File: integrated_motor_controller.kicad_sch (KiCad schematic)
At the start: 26 parts, among them J1 RCVR, J10 CH2, J2 SWD, J3 ENC 0, J4 ENC 1, J5 UART, J6 CH0, J7 I2C, J8 CH1, J9 I2C

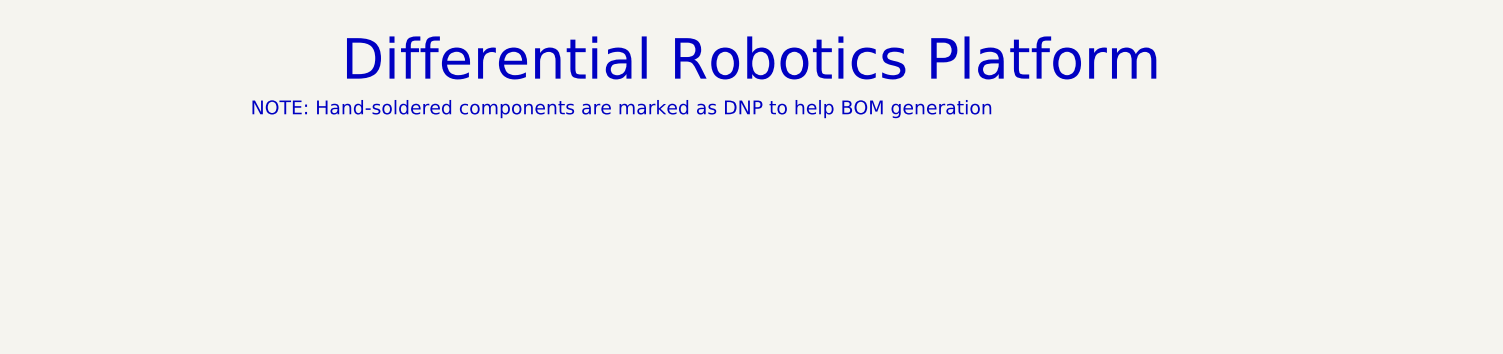
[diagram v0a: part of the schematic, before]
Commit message: Cleanup a comment in main schematic for the new project name
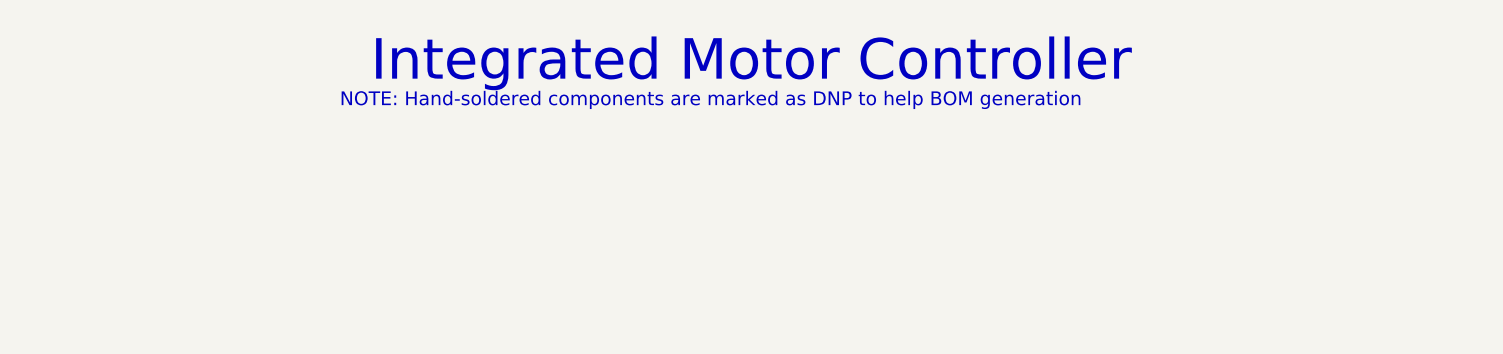
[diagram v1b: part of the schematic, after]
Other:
- note added: "Integrated Motor Controller"
- note removed: "Differential Robotics Platform"
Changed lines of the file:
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@@
 		)
 	)
-	(text "Differential Robotics Platform"
+	(text "Integrated Motor Controller"
 		(exclude_from_sim no)
 		(at 190.5 22.86 0)
@@
 	(text "NOTE: Hand-soldered components are marked as DNP to help BOM generation"
 		(exclude_from_sim no)
-		(at 134.874 28.194 0)
+		(at 144.78 27.178 0)
 		(effects
 			(font

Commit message: Final edits before sending to fab
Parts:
- added R2, R3: 3.3k, Resistor_SMD:R_0603_1608Metric, symbol Device:R_Small_US
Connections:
- net +3.3V: now also R2.2, R3.2
- net I2C_SCL: now also R2.1
- net I2C_SDA: now also R3.1
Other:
- sheet IMU: file imu_icm42688.kicad_sch -> imu_lsm6dsv.kicad_sch

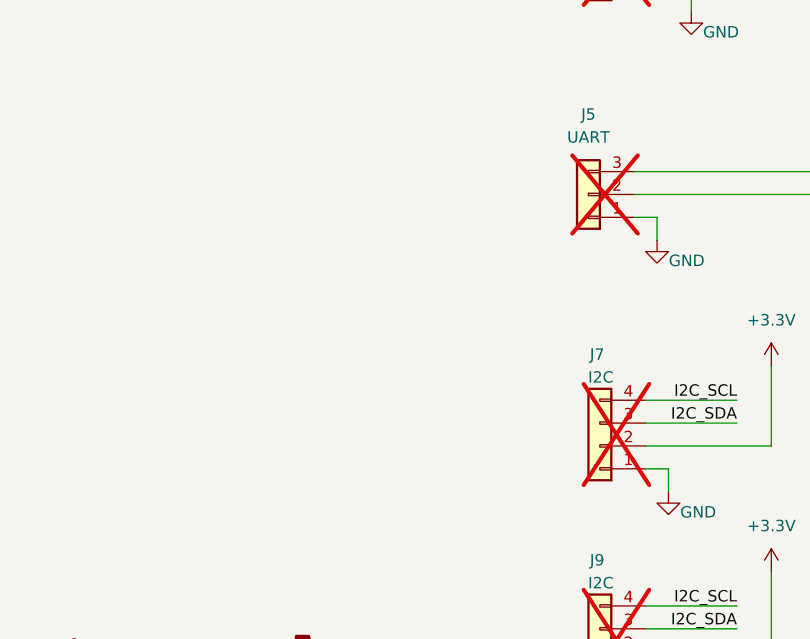
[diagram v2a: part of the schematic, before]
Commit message: Add comment on main sch for the mating connectors for I2C and UART
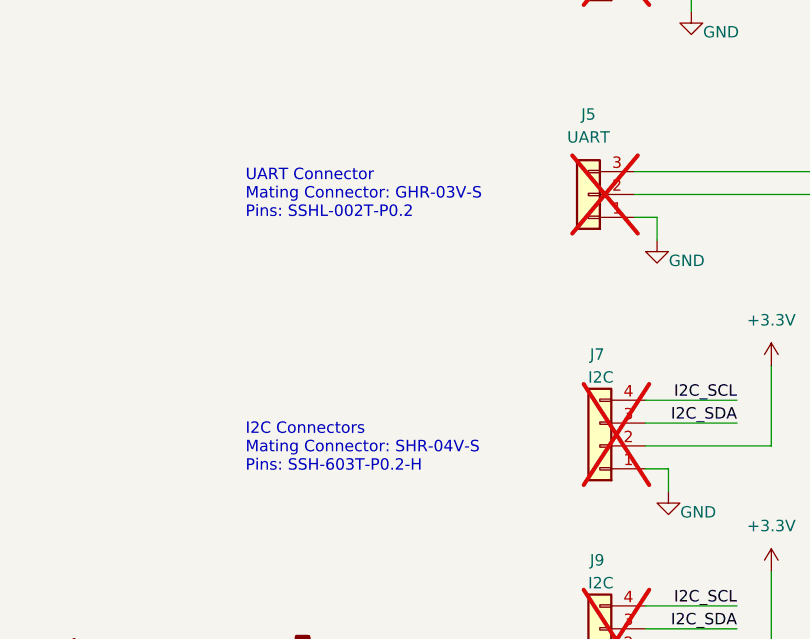
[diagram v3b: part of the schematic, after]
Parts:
- J7: MANUFACTURER (none) -> JST; Part No TODO -> BM04B-SRSS-TB
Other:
- note added: "I2C Connectors Mating Connector: SHR-04V-S Pins: SSH-603T-P0.2-H"
- note added: "UART Connector Mating Connector: GHR-03V-S Pins: SSHL-002T-P0.2"
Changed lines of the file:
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@@
 		)
 	)
+	(text "I2C Connectors\nMating Connector: SHR-04V-S\nPins: SSH-603T-P0.2-H"
+		(exclude_from_sim no)
+		(at 50.8 209.804 0)
+		(effects
+			(font
+				(size 1.27 1.27)
+			)
+			(justify left)
+		)
+	)
+	(text "UART Connector\nMating Connector: GHR-03V-S\nPins: SSHL-002T-P0.2"
+		(exclude_from_sim no)
+		(at 50.8 181.61 0)
+		(effects
+			(font
+				(size 1.27 1.27)
+			)
+			(justify left)
+		)
+	)
 	(text "NOTE: Hand-soldered components are marked as DNP to help BOM generation"
 		(exclude_from_sim no)
@@
 			)
 		)
-		(property "Part No" "TODO"
+		(property "Part No" "BM04B-SRSS-TB"
 			(at 90.17 209.55 0)
 			(hide yes)
@@
 			)
 		)
-		(property "MANUFACTURER" ""
+		(property "MANUFACTURER" "JST"
 			(at 90.17 209.55 0)
 			(hide yes)
